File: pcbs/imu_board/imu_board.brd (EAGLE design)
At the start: 58 x 58.3 mm, 25 parts, among them J1 RJ11-2L-B, U1 LSM9DS1, U2 ADP121-AUJZ33R7

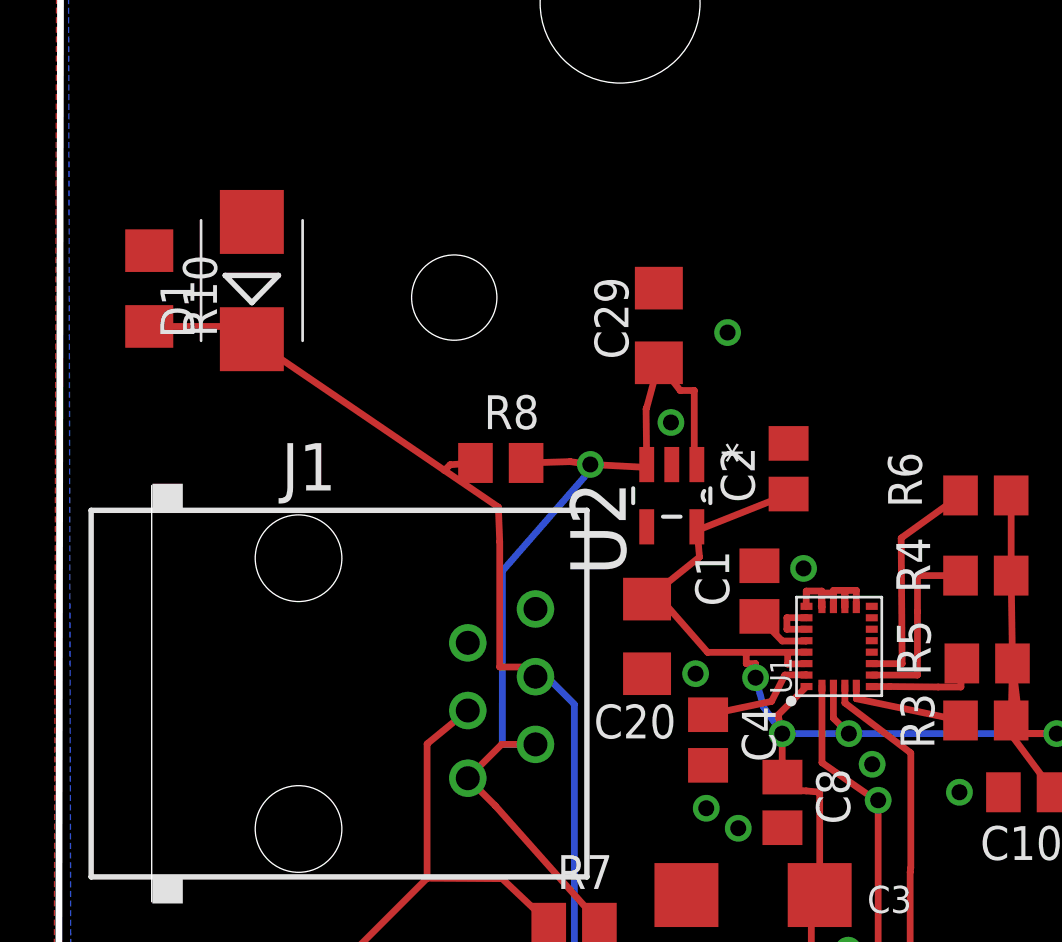
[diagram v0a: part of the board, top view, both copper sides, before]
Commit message: Added the dataready line
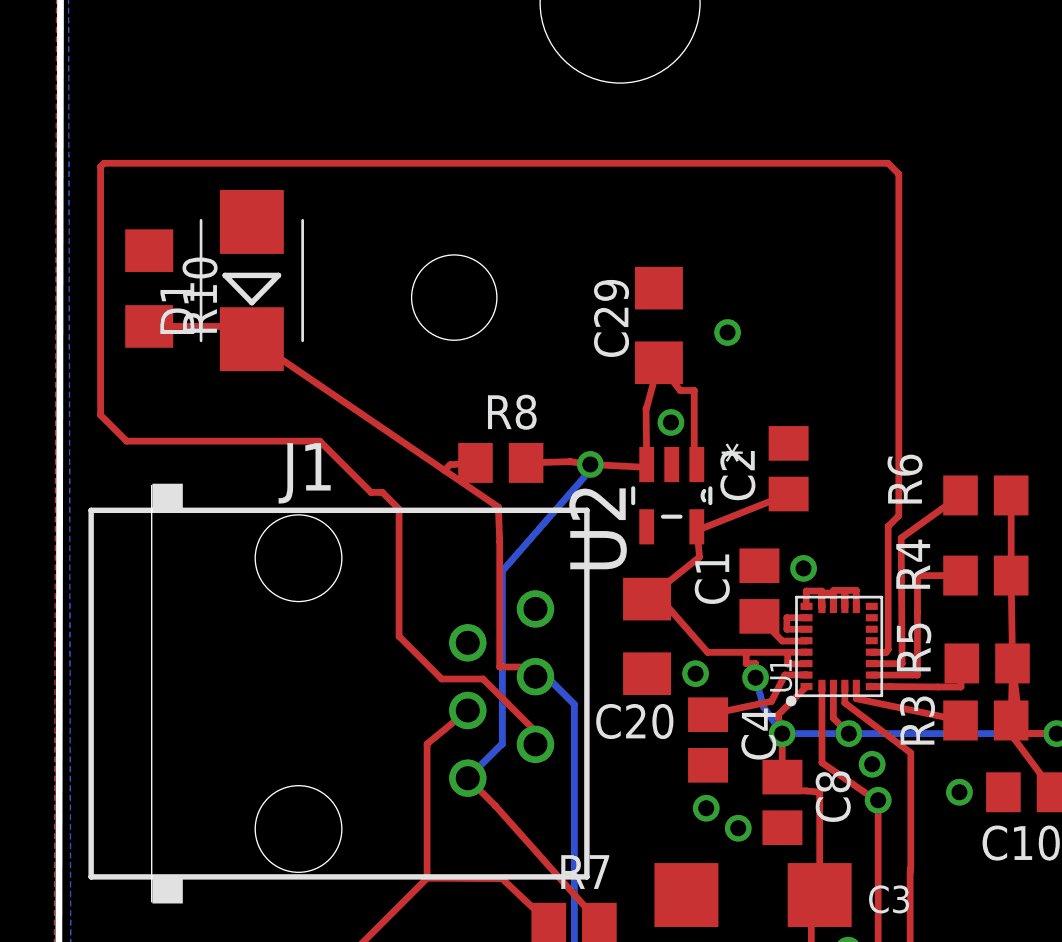
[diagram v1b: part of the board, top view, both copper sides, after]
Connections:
- new net N$3: J1.5, U1.9
- net N$46: no longer J1.5
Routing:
- net N$3: track 0.00 -> 82.7 mm
- net N$46: track 36.7 -> 34.2 mm
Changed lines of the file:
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@@
 <layer number="14" name="Route14" color="1" fill="6" visible="no" active="no"/>
 <layer number="15" name="Route15" color="4" fill="6" visible="no" active="no"/>
-<layer number="16" name="Bottom" color="1" fill="1" visible="yes" active="yes"/>
+<layer number="16" name="Bottom" color="1" fill="1" visible="no" active="yes"/>
 <layer number="17" name="Pads" color="2" fill="1" visible="yes" active="yes"/>
 <layer number="18" name="Vias" color="2" fill="1" visible="yes" active="yes"/>
@@
 </signal>
 <signal name="N$46">
-<contactref element="J1" pad="5"/>
 <contactref element="R8" pad="2"/>
 <contactref element="J1" pad="6"/>
@@
 <contactref element="U2" pad="3"/>
 <contactref element="U2" pad="1"/>
-<wire x1="18.542" y1="26.797" x2="17.272" y2="26.797" width="0.254" layer="1"/>
-<wire x1="17.272" y1="26.797" x2="16.002" y2="25.527" width="0.254" layer="1"/>
-<wire x1="18.542" y1="26.797" x2="17.297" y2="26.797" width="0.254" layer="16"/>
 <wire x1="17.297" y1="26.797" x2="17.3" y2="33.3" width="0.254" layer="16"/>
 <wire x1="17.3" y1="33.3" x2="20.7" y2="37.2" width="0.254" layer="16"/>
@@
 <wire x1="24.5" y1="40.075" x2="23.972" y2="40.075" width="0.254" layer="1"/>
 <wire x1="23.972" y1="40.075" x2="23.172" y2="41.115" width="0.254" layer="1"/>
+<wire x1="17.297" y1="26.797" x2="17.272" y2="26.797" width="0.254" layer="16"/>
+<wire x1="17.272" y1="26.797" x2="16.002" y2="25.527" width="0.254" layer="16"/>
 </signal>
 <signal name="N$9">
@@
 <wire x1="7.9" y1="42.478" x2="7.9" y2="42" width="0.254" layer="1"/>
 </signal>
+<signal name="N$3">
+<contactref element="J1" pad="5"/>
+<contactref element="U1" pad="9"/>
+<wire x1="18.542" y1="26.797" x2="18.542" y2="27.283" width="0.254" layer="1"/>
+<wire x1="18.542" y1="27.283" x2="16.575" y2="29.25" width="0.254" layer="1"/>
+<wire x1="16.575" y1="29.25" x2="15.025" y2="29.25" width="0.254" layer="1"/>
+<wire x1="15.025" y1="29.25" x2="13.425" y2="30.85" width="0.254" layer="1"/>
+<wire x1="13.425" y1="30.85" x2="13.425" y2="35.625" width="0.254" layer="1"/>
+<wire x1="13.425" y1="35.625" x2="12.8" y2="36.25" width="0.254" layer="1"/>
+<wire x1="12.8" y1="36.25" x2="12.375" y2="36.25" width="0.254" layer="1"/>
+<wire x1="12.375" y1="36.25" x2="10.45" y2="38.175" width="0.254" layer="1"/>
+<wire x1="10.45" y1="38.175" x2="3.2" y2="38.175" width="0.254" layer="1"/>
+<wire x1="3.2" y1="38.175" x2="2.225" y2="39.15" width="0.254" layer="1"/>
+<wire x1="2.225" y1="39.15" x2="2.225" y2="48.475" width="0.254" layer="1"/>
+<wire x1="2.225" y1="48.475" x2="2.35" y2="48.6" width="0.254" layer="1"/>
+<wire x1="2.35" y1="48.6" x2="31.775" y2="48.6" width="0.254" layer="1"/>
+<wire x1="31.775" y1="48.6" x2="32.175" y2="48.2" width="0.254" layer="1"/>
+<wire x1="32.175" y1="48.2" x2="32.175" y2="35.375" width="0.254" layer="1"/>
+<wire x1="32.175" y1="35.375" x2="31.775" y2="34.975" width="0.254" layer="1"/>
+<wire x1="31.775" y1="34.975" x2="31.775" y2="30.35" width="0.254" layer="1"/>
+<wire x1="31.775" y1="30.35" x2="31.7" y2="30.25" width="0.254" layer="1"/>
+<wire x1="31.7" y1="30.25" x2="31.179" y2="30.25" width="0.254" layer="1"/>
+<wire x1="31.179" y1="30.25" x2="31.161" y2="30.257" width="0.254" layer="1"/>
+</signal>
 </signals>

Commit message: Updated docs
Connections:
- net N$3: now also U1.12; no longer U1.9
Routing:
- net N$3: track 82.7 -> 81.4 mm
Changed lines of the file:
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@@
 <signal name="N$3">
 <contactref element="J1" pad="5"/>
-<contactref element="U1" pad="9"/>
 <wire x1="18.542" y1="26.797" x2="18.542" y2="27.283" width="0.254" layer="1"/>
 <wire x1="18.542" y1="27.283" x2="16.575" y2="29.25" width="0.254" layer="1"/>
@@
 <wire x1="32.175" y1="48.2" x2="32.175" y2="35.375" width="0.254" layer="1"/>
 <wire x1="32.175" y1="35.375" x2="31.775" y2="34.975" width="0.254" layer="1"/>
-<wire x1="31.775" y1="34.975" x2="31.775" y2="30.35" width="0.254" layer="1"/>
-<wire x1="31.775" y1="30.35" x2="31.7" y2="30.25" width="0.254" layer="1"/>
-<wire x1="31.7" y1="30.25" x2="31.179" y2="30.25" width="0.254" layer="1"/>
-<wire x1="31.179" y1="30.25" x2="31.161" y2="30.257" width="0.254" layer="1"/>
+<contactref element="U1" pad="12"/>
+<wire x1="31.161" y1="31.547" x2="31.775" y2="31.547" width="0.254" layer="1"/>
+<wire x1="31.775" y1="31.547" x2="31.775" y2="34.975" width="0.254" layer="1"/>
 </signal>
 </signals>
